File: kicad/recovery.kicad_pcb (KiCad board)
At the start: 2 copper layers, 84.1 x 61.7 mm, 42 parts, among them J1 Bus_PCI_Express_x1, J2 wago 2060-452/998-404, J3 wago 2060-452/998-404, J4 Conn_01x04, J6 USB_C_Receptacle_USB2.0_16P, U2 RP2040, U4 W25Q128JVP, U9 MCP25625T-E/ML, X1 RP2040 Crystal, Y2 X322516MLB4SI

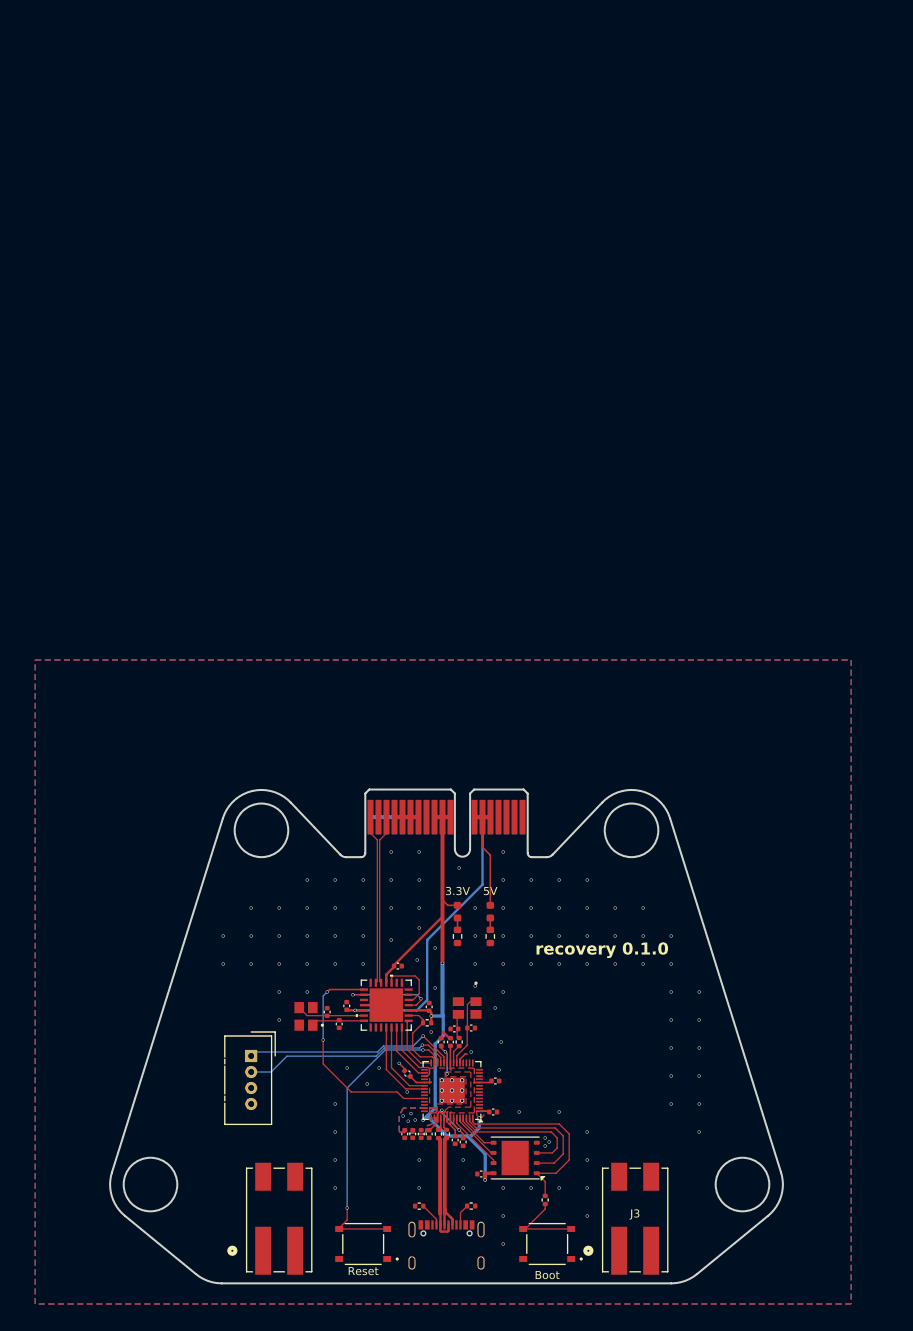
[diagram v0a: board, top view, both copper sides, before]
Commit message: rename symbol and footprint editor
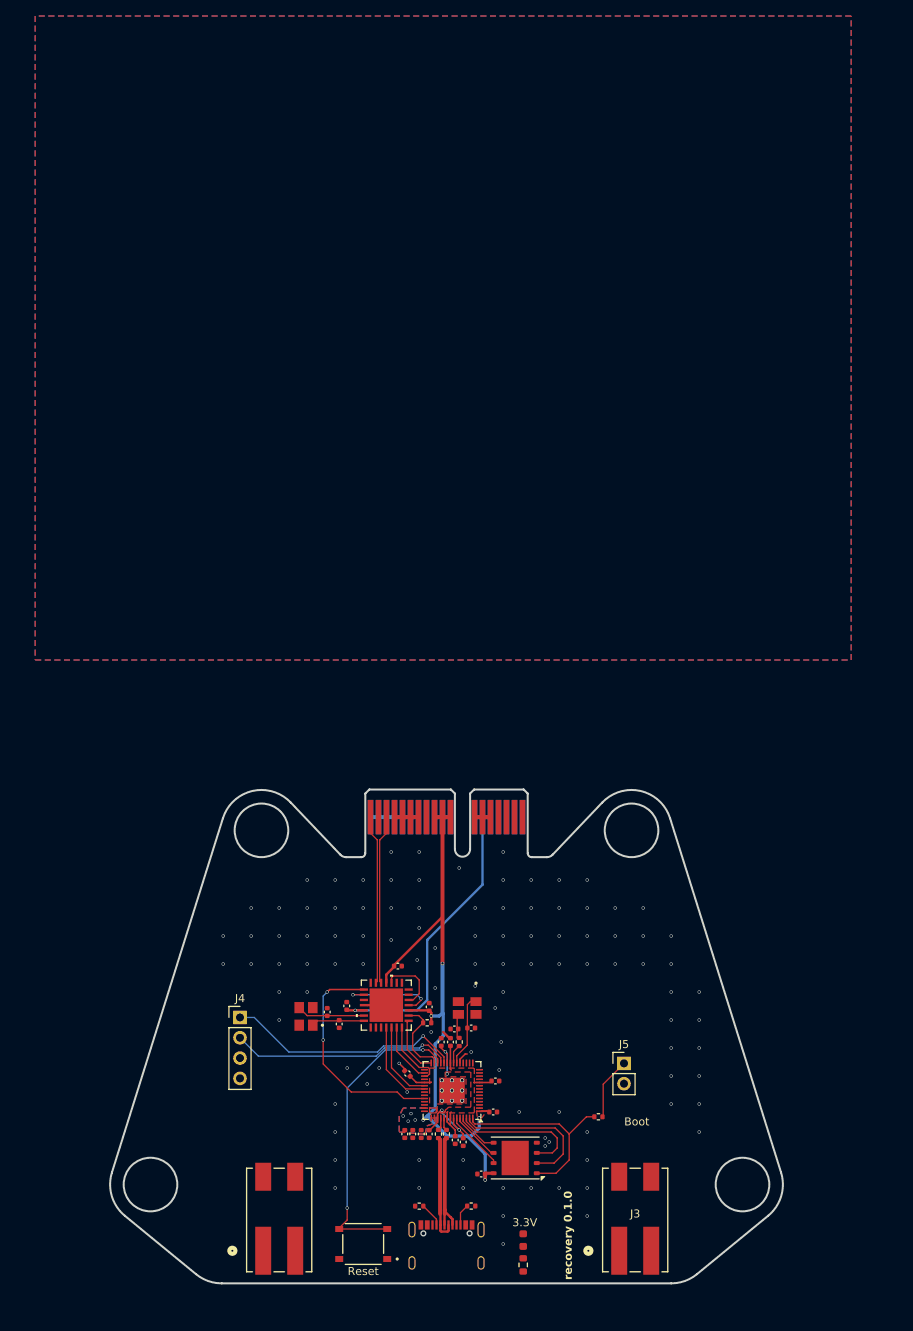
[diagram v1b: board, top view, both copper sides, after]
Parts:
- removed D2: LED, LED_SMD:LED_0603_1608Metric
- removed R2: 1k, Resistor_SMD:R_0603_1608Metric
- removed S1: TS-1187A-B-A-B, 4in-kicad-library:TS-1187A-B-A-B
- added J5: Conn_01x02_Pin, Connector_PinHeader_2.54mm:PinHeader_1x02_P2.54mm_Vertical, F.Cu at (168.6, 94.9)
- J4: footprint Connector:NS-Tech_Grove_1x04_P2mm_Vertical -> Connector_PinHeader_2.54mm:PinHeader_1x04_P2.54mm_Vertical
- moved D1 41.9 mm to (156.0, 117.0)
- moved R1 41.9 mm to (156.0, 120.1)
- moved R30 12.3 mm to (165.4, 101.6), turned to 0 degrees
- moved J4 5.02 mm to (120.6, 89.2)
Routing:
- net +5V: track 52.6 -> 41.2 mm
- net /SWCLK: track 27.0 -> 30.0 mm
- net /~{USB_BOOT_S}: track 10.4 -> 7.60 mm
- net +3.3V: track 101.3 -> 99.2 mm
- net /SWD: track 26.3 -> 27.8 mm
- net Net-(D2-K): track 1.49 -> 0.00 mm
- net Net-(D1-K): track 1.49 -> 0.00 mm
- net /QSPI_SS: track 24.4 -> 25.2 mm
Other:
- board text removed: "5V"

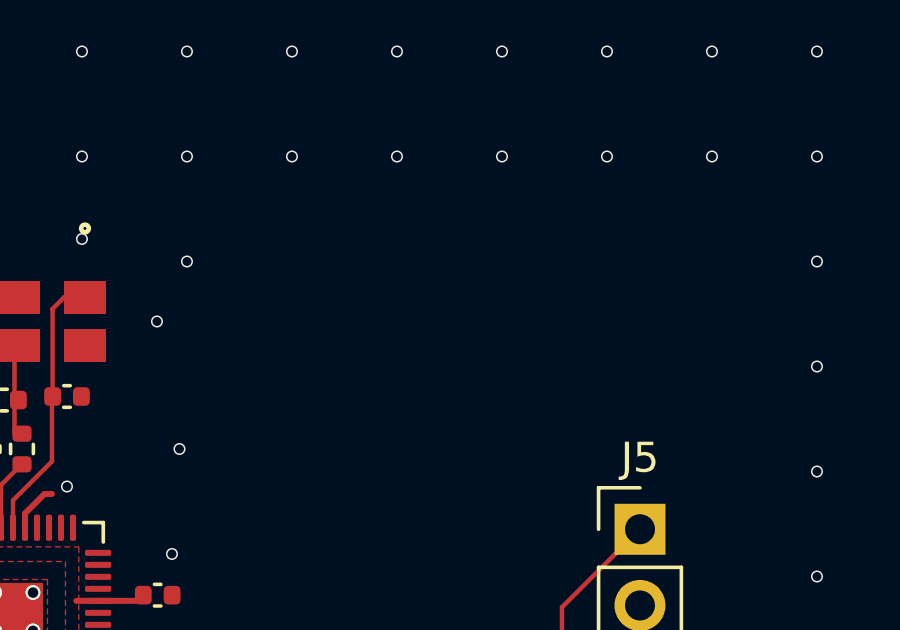
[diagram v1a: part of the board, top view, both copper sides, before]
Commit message: add dual N channel mosfet symbol and footprint
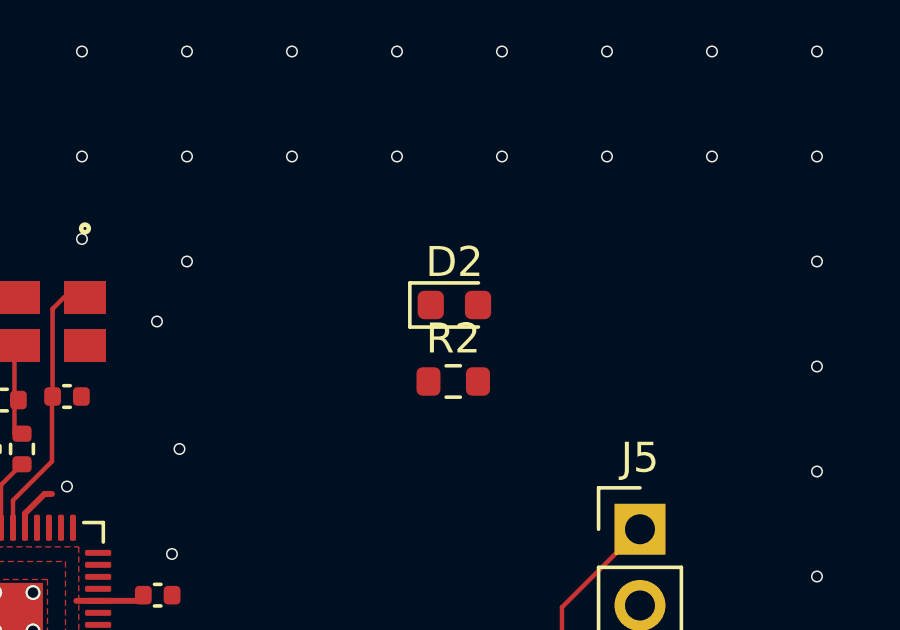
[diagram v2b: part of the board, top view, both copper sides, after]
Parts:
- added D2: LED, LED_SMD:LED_0603_1608Metric, F.Cu at (162.4, 87.5)
- added R2: 1k, Resistor_SMD:R_0603_1608Metric, F.Cu at (162.4, 90.0)

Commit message: begin fet routing
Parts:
- removed D2: LED, LED_SMD:LED_0603_1608Metric
- removed R2: 1k, Resistor_SMD:R_0603_1608Metric
- added Q1: SI7232DN-T1-GE3, 4in-recovery:SI7232DN-T1-GE3, F.Cu at (164.3, 96.1)
- added R20: 100, Resistor_SMD:R_0402_1005Metric, F.Cu at (159.6, 97.2)
- added R21: 3.3k, Resistor_SMD:R_0402_1005Metric, F.Cu at (159.1, 98.9)
- added R22: 100k, Resistor_SMD:R_0402_1005Metric, F.Cu at (169.9, 98.0)
- added R23: 27k, Resistor_SMD:R_0402_1005Metric, F.Cu at (169.9, 100.9)
- added R300: 100, Resistor_SMD:R_0402_1005Metric, F.Cu at (157.5, 91.1)
- added R31: 3.3k, Resistor_SMD:R_0402_1005Metric, F.Cu at (157.5, 85.1)
- added R32: 100k, Resistor_SMD:R_0402_1005Metric, F.Cu at (157.5, 87.1)
- added R33: 27k, Resistor_SMD:R_0402_1005Metric, F.Cu at (157.5, 89.1)
- J2, J3: footprint recovery:wago-2060-452_998-404 -> 4in-recovery:wago-2060-452_998-404
- moved J5 41.3 mm to (200.4, 68.6)
- moved R30 41.3 mm to (197.2, 75.3)
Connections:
- J1 pad A16: unconnected-(J1-PERp0-PadA16) -> v_lipo
- J1 pad A17: unconnected-(J1-PERn0-PadA17) -> v_lipo
- J1 pad A18: unconnected-(J1-GND-PadA18) -> v_lipo
- J1 pad B16: unconnected-(J1-GND-PadB16) -> v_lipo
- J1 pad B17: unconnected-(J1-~{PRSNT2}-PadB17) -> v_lipo
- J1 pad B18: unconnected-(J1-GND-PadB18) -> v_lipo
- J2 pad 1: unconnected-(J2-1_1-Pad1) -> Net-(J2-1_1)
- J2 pad 2: unconnected-(J2-1_2-Pad2) -> Net-(J2-1_1)
- J2 pad 3: unconnected-(J2-2_1-Pad3) -> v_lipo
- J2 pad 4: unconnected-(J2-2_2-Pad4) -> v_lipo
- J3 pad 1: unconnected-(J3-1_1-Pad1) -> Net-(J3-1_1)
- J3 pad 2: unconnected-(J3-1_2-Pad2) -> Net-(J3-1_1)
- J3 pad 3: unconnected-(J3-2_1-Pad3) -> v_lipo
- J3 pad 4: unconnected-(J3-2_2-Pad4) -> v_lipo
- U2 pad 2: unconnected-(U2-GPIO0-Pad2) -> fire_m
- U2 pad 3: unconnected-(U2-GPIO1-Pad3) -> fire_d
- U2 pad 4: unconnected-(U2-GPIO2-Pad4) -> sense_d
- U2 pad 5: unconnected-(U2-GPIO3-Pad5) -> sense_m
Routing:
- net fire_d: track 0.00 -> 10.5 mm
- net /~{USB_BOOT_S}: track 7.60 -> 0.00 mm
- net Net-(J3-1_1): track 0.00 -> 4.13 mm
- net /QSPI_SS: track 25.2 -> 21.1 mm
- net Net-(Q1-Pad4): track 0.00 -> 2.84 mm
- net GND: vias 117 -> 96

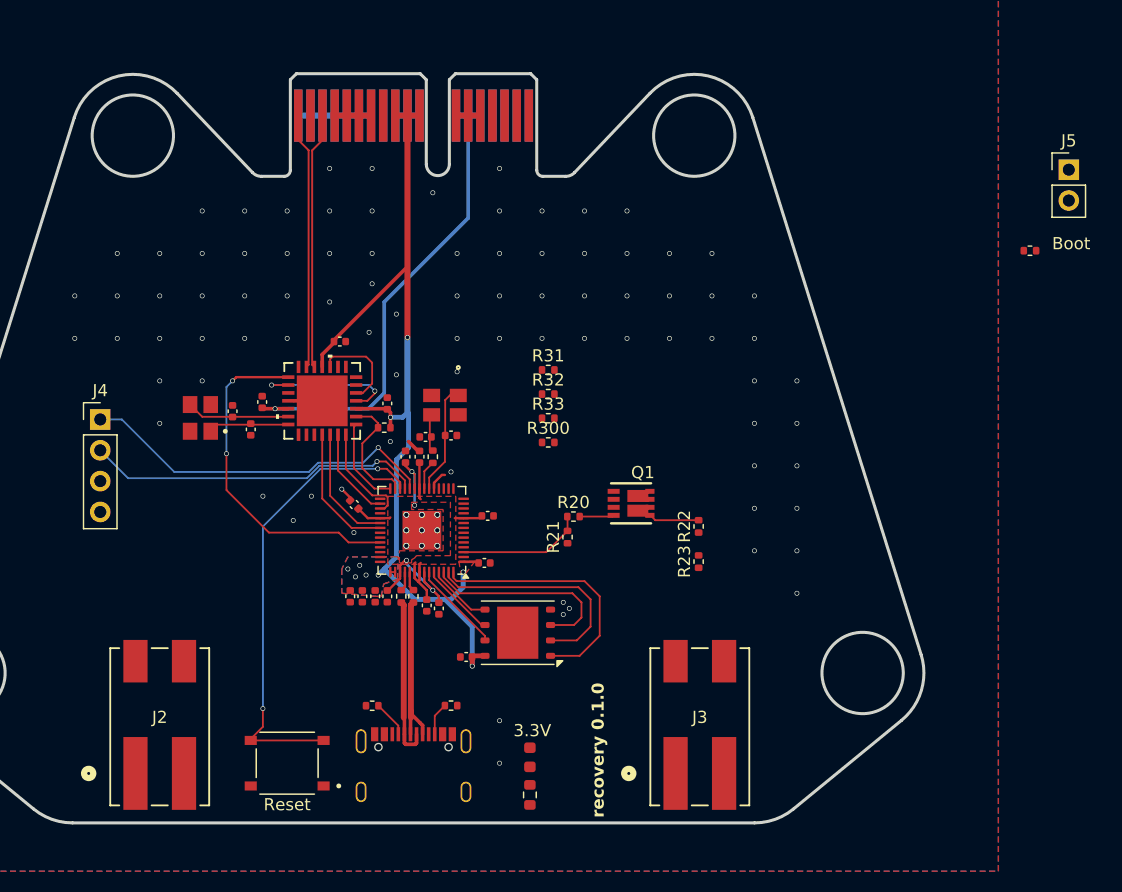
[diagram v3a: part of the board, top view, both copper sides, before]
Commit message: fix outline
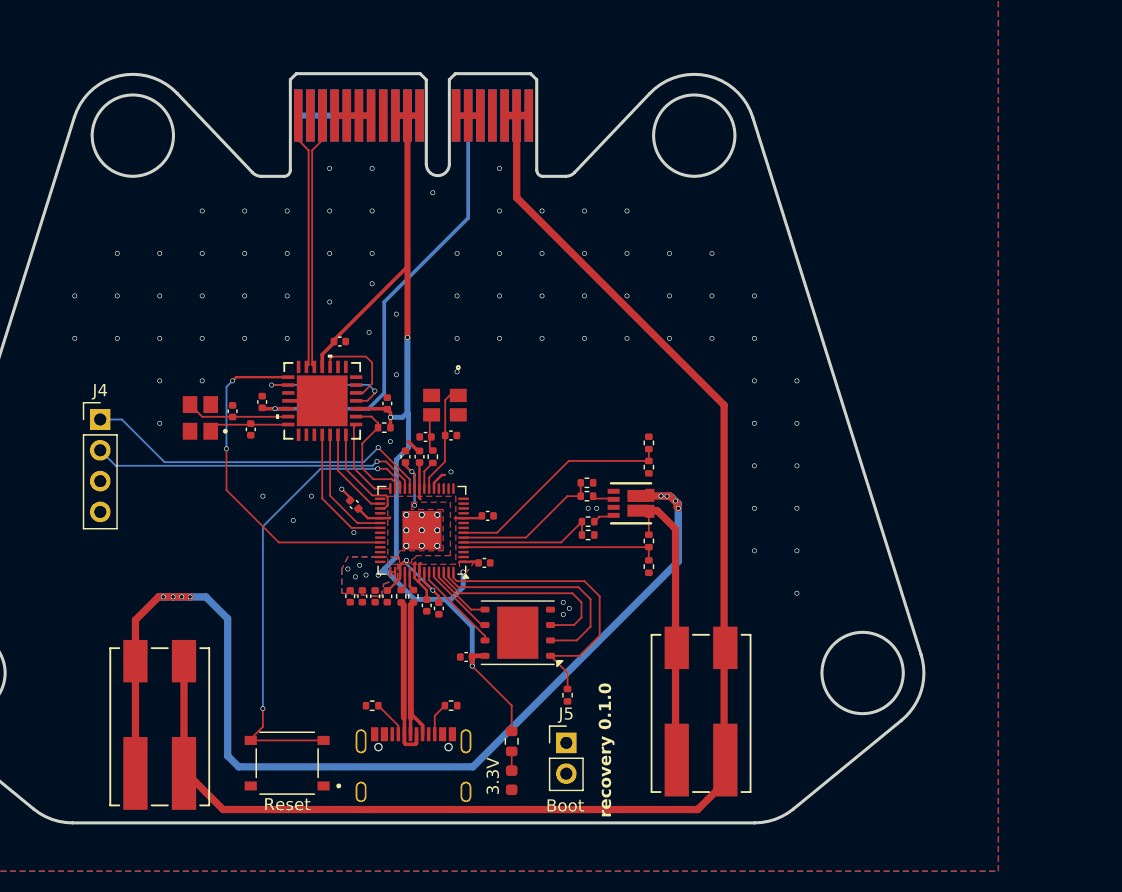
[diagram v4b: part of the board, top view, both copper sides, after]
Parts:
- Q1: value SI7232DN-T1-GE3 -> TRANS_SI7232DN-T1-GE3
- moved J5 62.8 mm to (159.0, 115.8)
- moved R30 52.8 mm to (159.1, 111.9), turned to -90 degrees
- moved R32 10.2 mm to (165.8, 93.1), turned to -90 degrees
- moved R31 9.83 mm to (160.7, 94.4), turned to 180 degrees
- moved R33 8.53 mm to (165.8, 91.1), turned to -90 degrees
- moved R300 5.46 mm to (160.7, 95.5)
- moved R1 4.66 mm to (154.5, 115.7)
- moved R22 4.27 mm to (165.8, 99.2)
- moved R23 4.12 mm to (165.8, 101.3)
- moved D1 2.41 mm to (154.5, 118.9)
- moved R21 1.71 mm to (160.8, 98.7), turned to 180 degrees
- moved R20 1.28 mm to (160.8, 97.6)
- moved J3 1.10 mm to (170.1, 113.4)
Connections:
- D1 pad 1: Net-(D1-K) -> GND
- D1 pad 2: +3.3V -> Net-(D1-A)
- R1 pad 1: Net-(D1-K) -> +3.3V
- R1 pad 2: GND -> Net-(D1-A)
- U2 pad 2: fire_m -> unconnected-(U2-GPIO0-Pad2)
- U2 pad 3: fire_d -> unconnected-(U2-GPIO1-Pad3)
- U2 pad 5: sense_m -> fire_d
- U2 pad 6: unconnected-(U2-GPIO4-Pad6) -> fire_m
- U2 pad 7: unconnected-(U2-GPIO5-Pad7) -> sense_m
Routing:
- net v_lipo: track 0.00 -> 122.1 mm
- net Net-(J2-1_1): track 0.00 -> 90.7 mm, vias 0 -> 8
- net Net-(J3-1_1): track 4.13 -> 24.5 mm
- net sense_m: track 0.00 -> 18.7 mm
- net sense_d: track 0.00 -> 16.4 mm
- net fire_m: track 0.03 -> 12.2 mm
- net +3.3V: track 99.2 -> 105.9 mm
- net /QSPI_SS: track 21.1 -> 24.5 mm
- net Net-(Q1-Pad2): track 0.00 -> 1.80 mm
- net Net-(D1-A): track 0.00 -> 1.59 mm
- net fire_d: track 10.5 -> 11.6 mm
- net Net-(Q1-Pad4): track 2.84 -> 1.81 mm
- net /SWD: track 27.8 -> 27.0 mm
- net /SWCLK: track 30.0 -> 29.3 mm

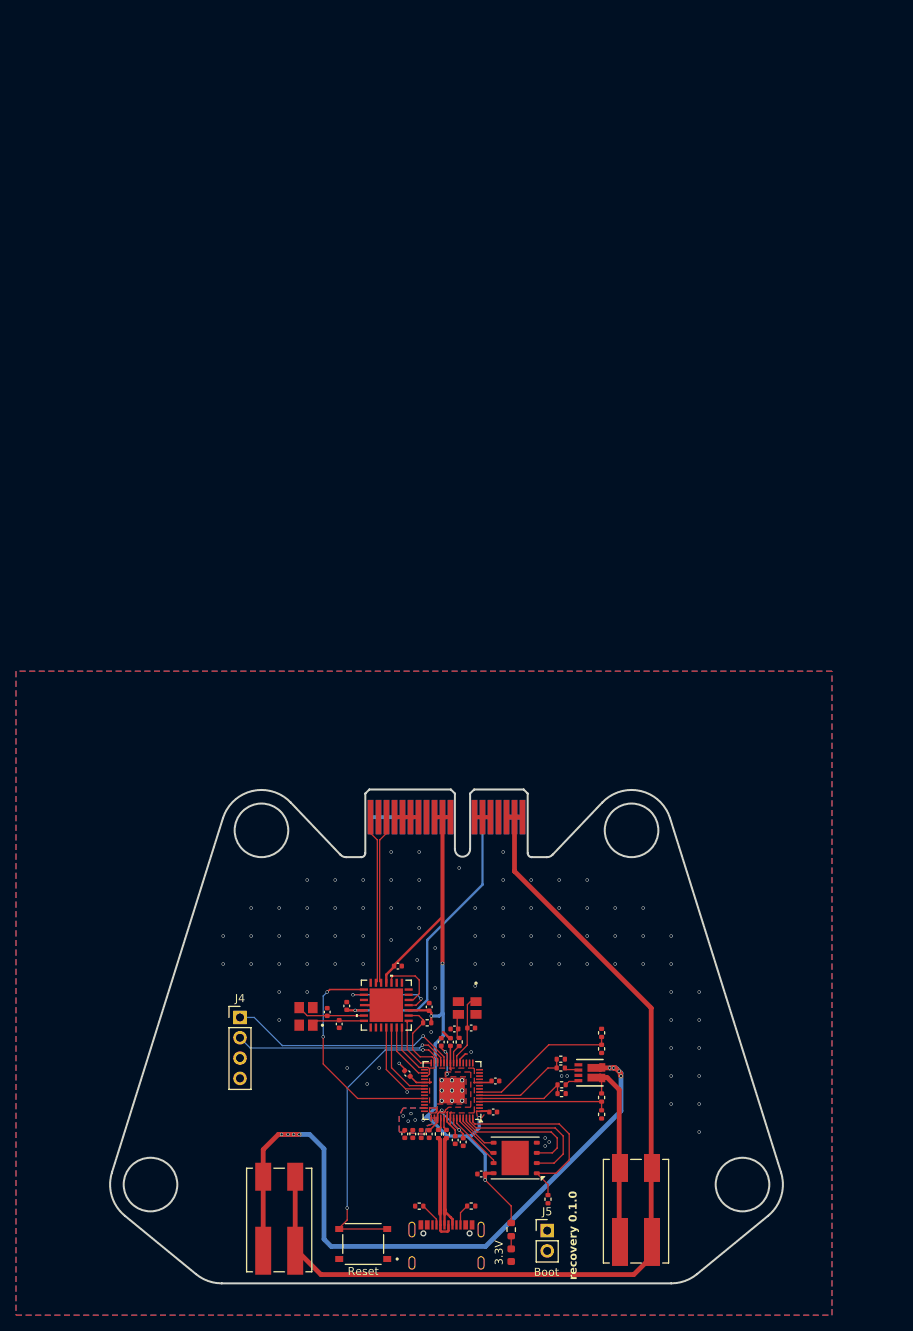
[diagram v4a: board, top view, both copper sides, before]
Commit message: update PCIe footprint
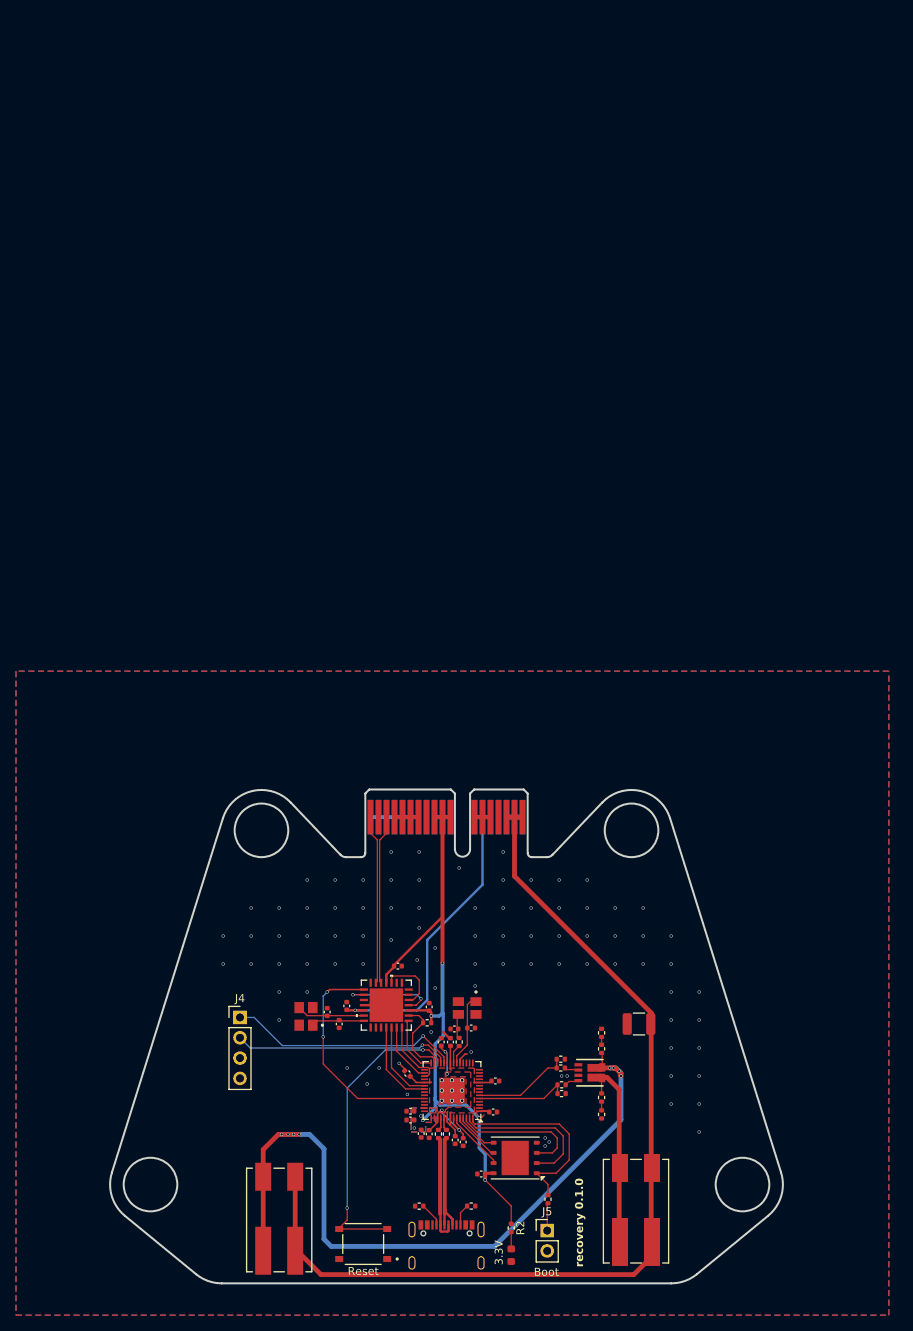
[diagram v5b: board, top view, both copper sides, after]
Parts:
- removed R1: 1k, Resistor_SMD:R_0603_1608Metric
- added C1: 100u, Capacitor_SMD:C_1210_3225Metric, F.Cu at (170.5, 90.0)
- added R2: 1k, Resistor_SMD:R_0402_1005Metric, F.Cu at (154.5, 115.5)
- Q1: value TRANS_SI7232DN-T1-GE3 -> SI7232DN-T1-GE3
- moved C215 2.94 mm to (141.9, 100.9), turned to 180 degrees
- moved C216 1.77 mm to (141.9, 102.0), turned to 180 degrees
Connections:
- net +1.1V renamed +1V1
- net CANN renamed CANL
- net CANP renamed CANH
- net USB_D+ renamed /USB_D+
- net USB_D- renamed /USB_D-
- U2 pad 39: unconnected-(U2-GPIO27_ADC1-Pad39) -> sense_d
- U2 pad 4: sense_d -> unconnected-(U2-GPIO2-Pad4)
- U2 pad 40: unconnected-(U2-GPIO28_ADC2-Pad40) -> sense_m
- U2 pad 7: sense_m -> unconnected-(U2-GPIO5-Pad7)
- U4 pad 9: (no net) -> unconnected-(U4-EP-Pad9)
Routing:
- net sense_m: track 18.7 -> 0.98 mm
- net sense_d: track 16.4 -> 1.09 mm
- net /~{USB_BOOT_S}: track 0.00 -> 3.46 mm
- net Net-(J2-1_1): track 90.7 -> 92.9 mm
- net +3.3V: track 105.9 -> 105.3 mm, vias 9 -> 7
- net Net-(D1-A): track 1.59 -> 2.11 mm
